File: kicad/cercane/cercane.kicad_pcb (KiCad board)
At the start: 2 copper layers, 2 parts, among them U1 ATtiny45-20SU, U2 NRF24L01_Breakout

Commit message: new PCB
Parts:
- added C1: 100nF, Capacitor_SMD:C_1206_3216Metric, F.Cu at (179.1, 58.4)
- added J1: Conn_02x03_Odd_Even, Connector_PinSocket_2.54mm:PinSocket_2x03_P2.54mm_Vertical_SMD, F.Cu at (171.2, 61.6)
- U1: value ATtiny45-20SU -> ATtiny45-20PU; footprint ATTINY85-20SU:SOIC127P798X216-8N -> ATTINY45-20PU:DIP787W46P254L927H533Q8
- moved U1 25.4 mm to (174.0, 76.2), turned to 90 degrees
- moved U2 2.05 mm to (156.2, 71.1)
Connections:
- net Net-(U1-Pad6) renamed /MISO
- net VCC renamed +3V3
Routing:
- net Net-(U1-Pad3): track 7.74 -> 68.3 mm
- net GND: track 0.00 -> 25.3 mm
- net Net-(U1-Pad5): track 21.1 -> 0.00 mm
- net +3V3: track 0.00 -> 11.9 mm
- net /MISO: track 8.10 -> 0.00 mm
- net Net-(U1-Pad7): track 6.68 -> 0.00 mm
- net Net-(U1-Pad2): track 18.4 -> 16.7 mm
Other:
- board outline added: 74.9 x 33 mm
- net class Default: trace_width 0.25 -> 0.4
- rule trace_min: 0.2 -> 0.3

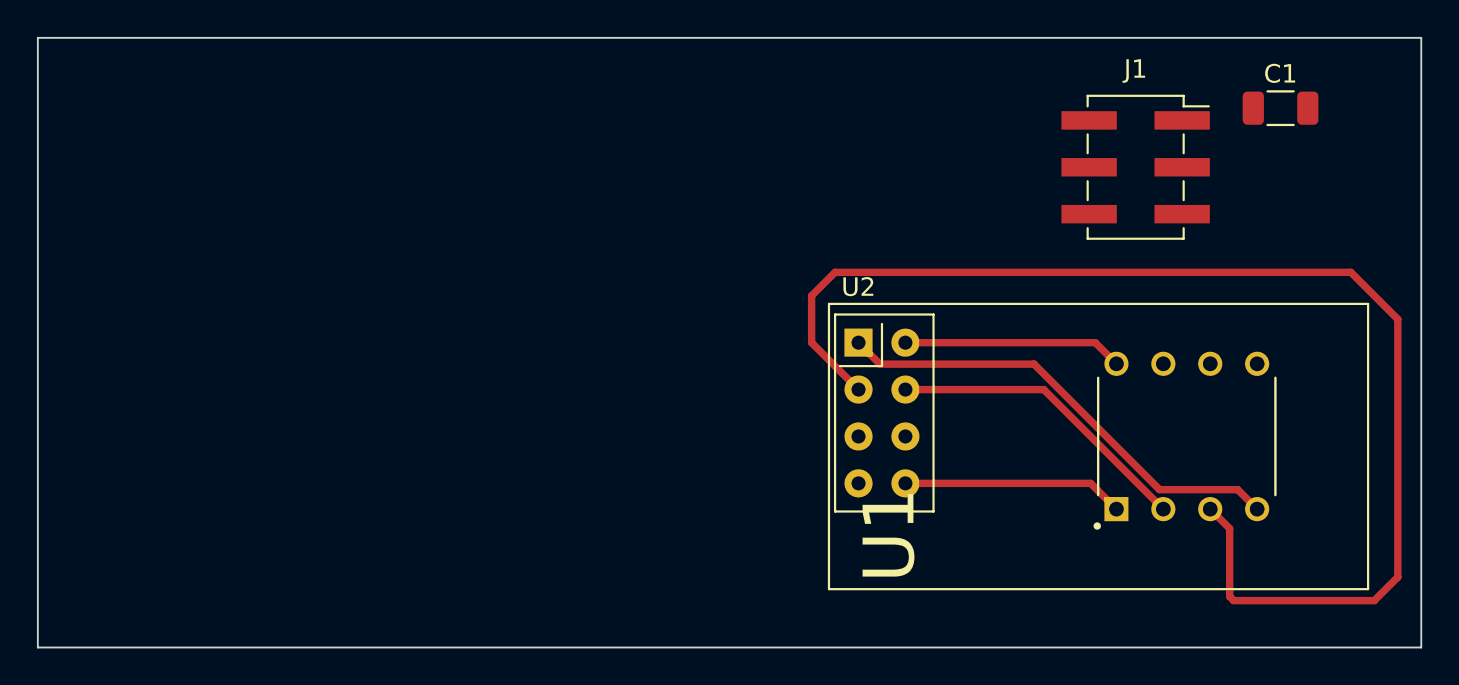
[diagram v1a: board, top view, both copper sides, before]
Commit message: new components on PCB
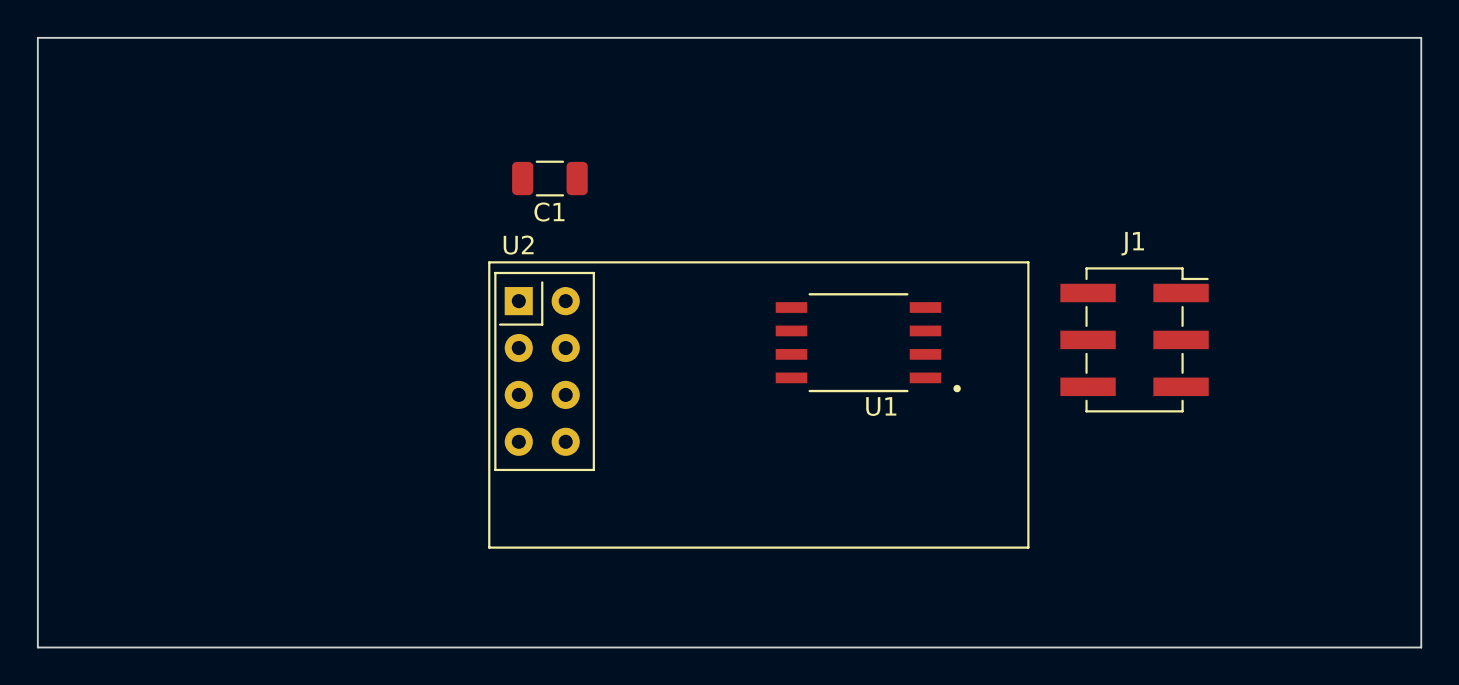
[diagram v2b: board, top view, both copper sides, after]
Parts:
- U1: footprint ATTINY45-20PU:DIP787W46P254L927H533Q8 -> ATTINY85-20SU:SOIC127P798X216-8N
- moved C1 39.8 mm to (139.5, 62.2), turned to 180 degrees
- moved U2 18.5 mm to (137.8, 68.9)
- moved U1 18.5 mm to (156.2, 71.1), turned to 180 degrees
- moved J1 9.35 mm to (171.2, 71.0)
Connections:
- J1 pad 2: Net-(J1-Pad2) -> +3V3
- J1 pad 3: Net-(J1-Pad3) -> /SCK
- J1 pad 4: Net-(J1-Pad4) -> /MOSI
- J1 pad 5: Net-(J1-Pad5) -> /RST
- J1 pad 6: Net-(J1-Pad6) -> GND
- U1 pad 1: Net-(U1-Pad1) -> /RST
- U1 pad 5: Net-(U1-Pad5) -> /MOSI
- U1 pad 7: Net-(U1-Pad7) -> /SCK
- U2 pad 5: Net-(U1-Pad7) -> /SCK
- U2 pad 6: Net-(U1-Pad5) -> /MOSI
- U2 pad 8: Net-(U1-Pad1) -> /RST
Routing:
- net Net-(U1-Pad3): track 68.3 -> 0.00 mm
- net GND: track 25.3 -> 0.00 mm
- net Net-(U1-Pad2): track 16.7 -> 0.00 mm
- net Net-(U1-Pad1): track 12.0 -> 0.00 mm
- net +3V3: track 11.9 -> 0.00 mm

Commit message: Exported PCB in png and svg
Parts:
- moved J1 23.0 mm to (149.9, 62.2)
- moved U1 18.9 mm to (139.9, 61.6), turned to 0 degrees
- moved C1 4.58 mm to (142.0, 66.0), turned to 0 degrees
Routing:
- net /SCK: track 0.00 -> 63.6 mm
- net /RST: track 0.00 -> 44.1 mm
- net /MISO: track 0.00 -> 32.0 mm
- net GND: track 0.00 -> 27.8 mm
- net /MOSI: track 0.00 -> 21.9 mm
- net +3V3: track 0.00 -> 19.5 mm
- net Net-(U1-Pad2): track 0.00 -> 13.4 mm
- net Net-(U1-Pad3): track 0.00 -> 11.1 mm
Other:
- board size 74.9 x 33 mm -> 34.3 x 27.9 mm
- net class Default: trace_width 0.4 -> 0.3
- board text added: "Cercane v.0.1"
